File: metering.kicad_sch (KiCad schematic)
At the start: 1 part, among them U1 NodeMCU v2

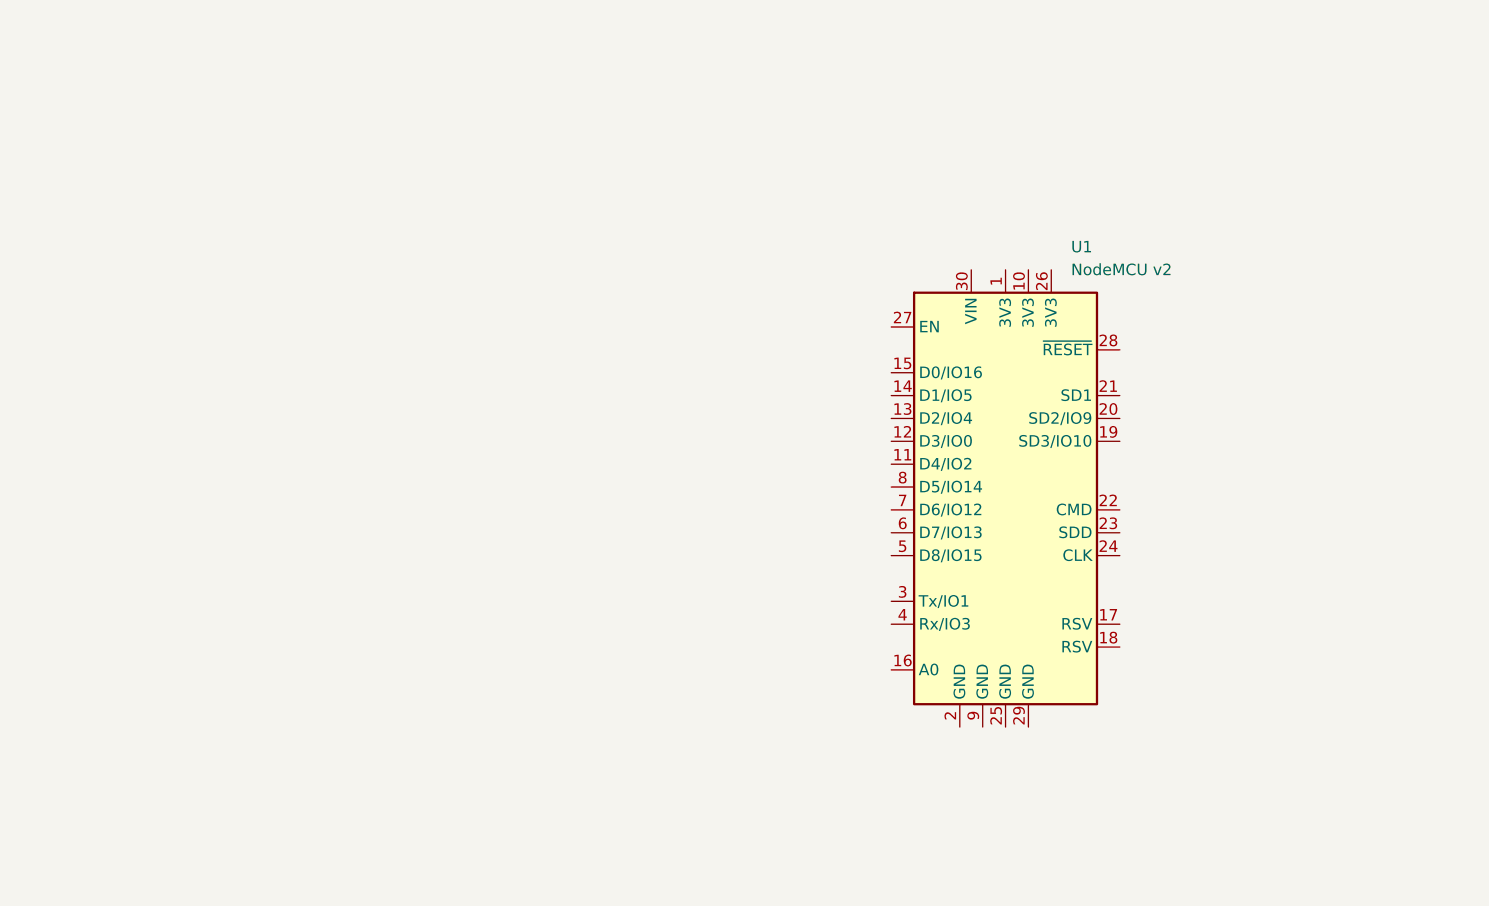
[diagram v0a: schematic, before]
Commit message: Add schematics for electric and gas meter as built in 11/2022
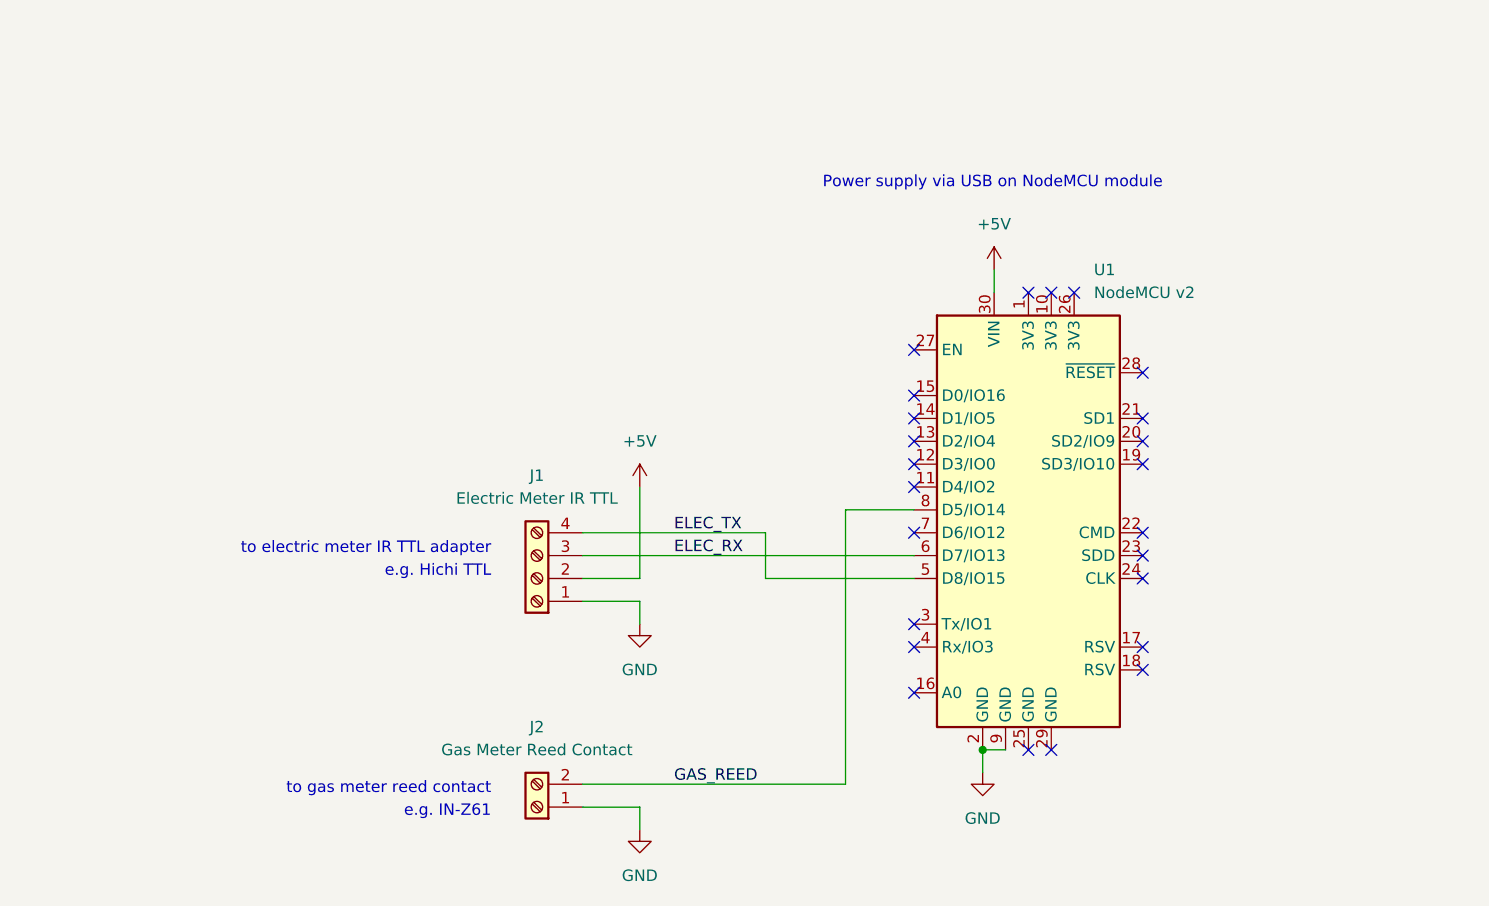
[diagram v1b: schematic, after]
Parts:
- added J1: Electric Meter IR TTL, Connector_PinSocket_2.54mm:PinSocket_1x04_P2.54mm_Vertical, symbol Connector:Screw_Terminal_01x04
- added J2: Gas Meter Reed Contact, Connector_PinSocket_2.54mm:PinSocket_1x02_P2.54mm_Vertical, symbol Connector:Screw_Terminal_01x02
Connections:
- net GND: now reaches U1.2 (GND)
- net GND: now also U1.9 (GND), J1.1 (Pin_1), J2.1 (Pin_1)
- net +5V: now reaches U1.30 (VIN)
- net +5V: now also J1.2 (Pin_2)
- net ELEC_TX: now reaches U1.5 (D8/IO15)
- net ELEC_TX: now also J1.4 (Pin_4)
- net ELEC_RX: now reaches U1.6 (D7/IO13)
- net ELEC_RX: now also J1.3 (Pin_3)
- net GAS_REED: now reaches U1.8 (D5/IO14)
- net GAS_REED: now also J2.2 (Pin_2)
- no-connect marks 0 -> 24
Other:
- note added: "Power supply via USB on NodeMCU module"
- note added: "e.g. Hichi TTL"
- note added: "e.g. IN-Z61"
- note added: "to electric meter IR TTL adapter"
- note added: "to gas meter reed contact"
- title: Smart Home Metering -> Smart Home Energy Metering
- moved on the sheet: U1

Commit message: Add NodeMCU footprint
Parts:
- U1: footprint Module:Arduino_Nano -> NodeMCU_v2:NodeMCU_v2; symbol NodeMCU v2:NodeMCU v2 -> NodeMCU_v2:NodeMCU_v2
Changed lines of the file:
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@@
     )
   )
-  (symbol (lib_id "NodeMCU v2:NodeMCU v2") (at 144.78 82.55 0) (unit 1)
+  (symbol (lib_id "NodeMCU_v2:NodeMCU_v2") (at 144.78 82.55 0) (unit 1)
     (in_bom yes) (on_board yes) (dnp no) (fields_autoplaced)
     (property "Reference" "U1" (at 152.0541 54.61 0)
@@
       (effects (font (size 1.27 1.27)) (justify left))
     )
-    (property "Footprint" "Module:Arduino_Nano" (at 144.78 82.55 0)
+    (property "Footprint" "NodeMCU_v2:NodeMCU_v2" (at 144.78 121.92 0)
       (effects (font (size 1.27 1.27) italic) hide)
     )
-    (property "Datasheet" "https://www.nodemcu.com/index_en.html" (at 144.78 82.55 0)
+    (property "Datasheet" "https://www.nodemcu.com/index_en.html" (at 144.78 119.38 0)
       (effects (font (size 1.27 1.27)) hide)
     )

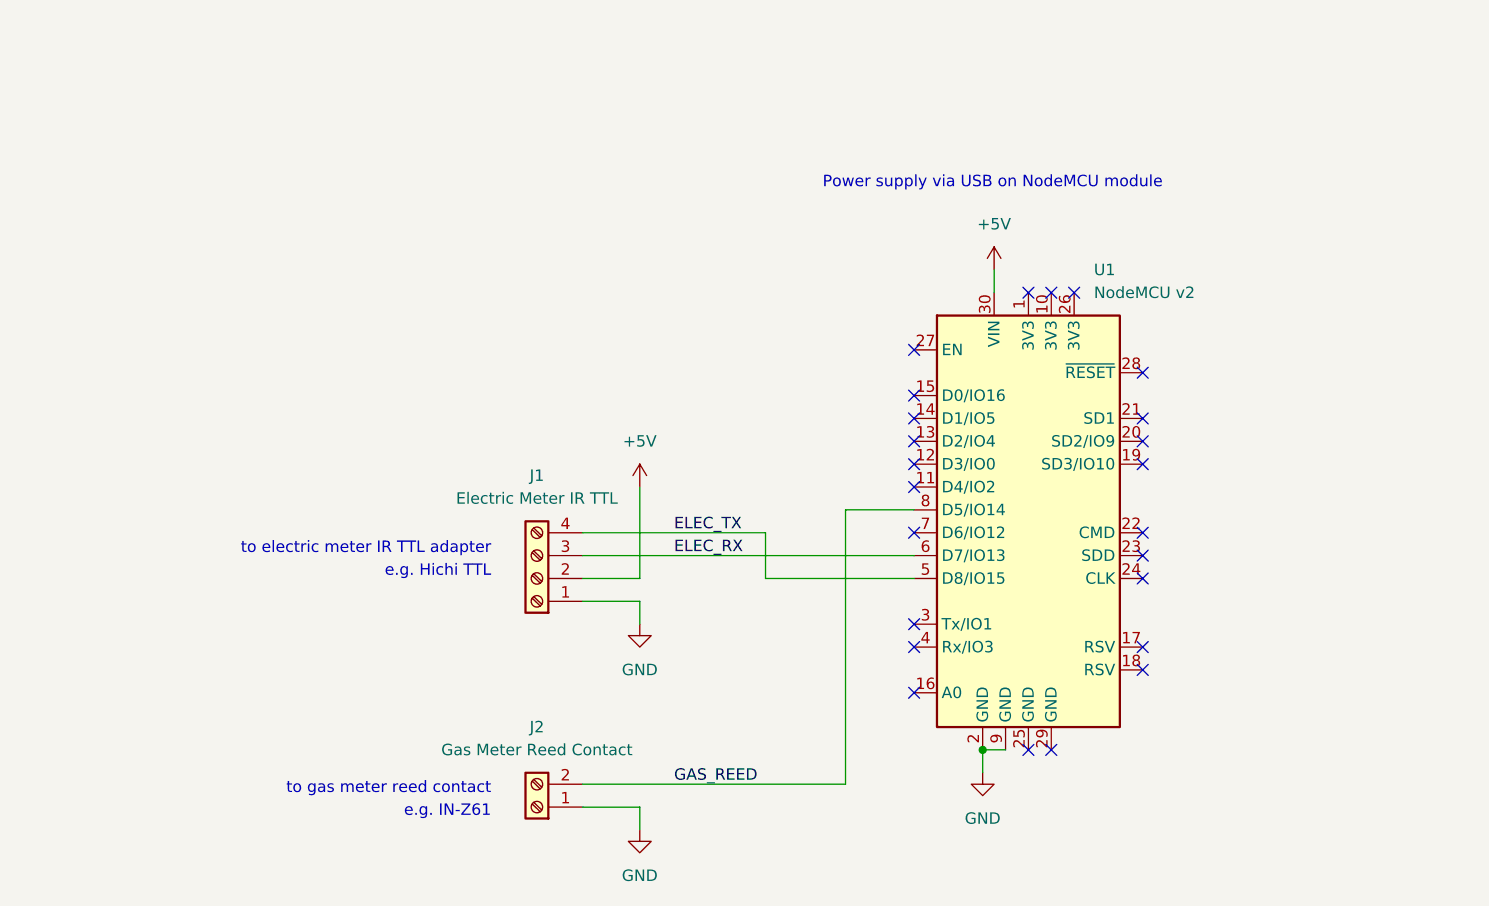
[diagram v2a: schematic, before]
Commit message: Add reed debounce circuit
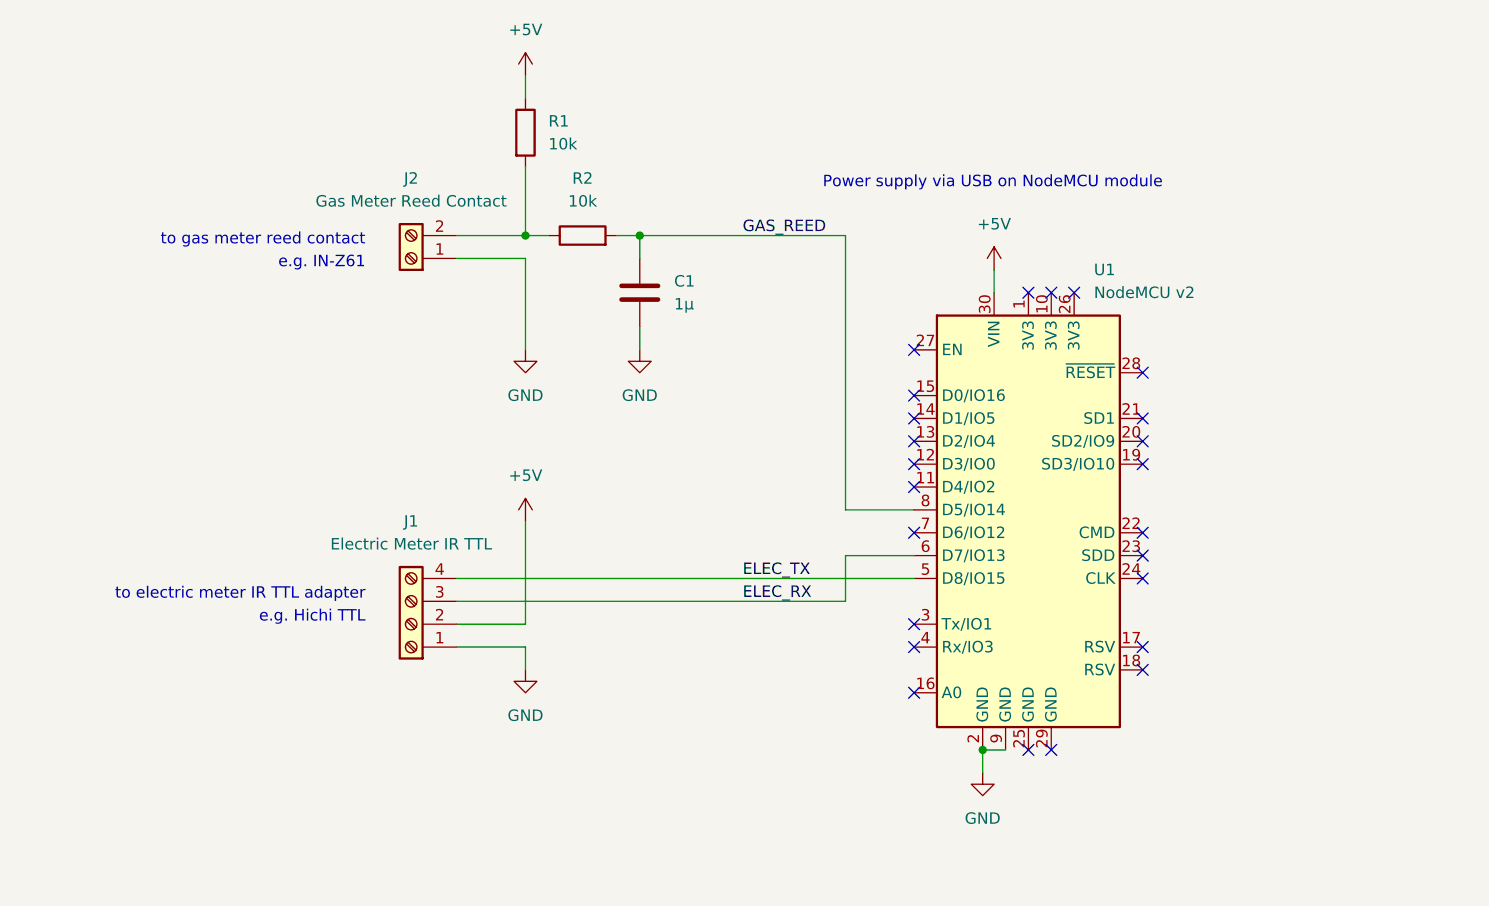
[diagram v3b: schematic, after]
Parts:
- added C1: 1µ, symbol Device:C
- added R1, R2: 10k, symbol Device:R
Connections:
- net +5V: now also R1.1
- net GAS_REED: now also C1.1, R2.2; no longer J2.2 (Pin_2)
- net GND: now also C1.2
- new net: J2.2 (Pin_2), R1.2, R2.1
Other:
- moved on the sheet: J1, J2

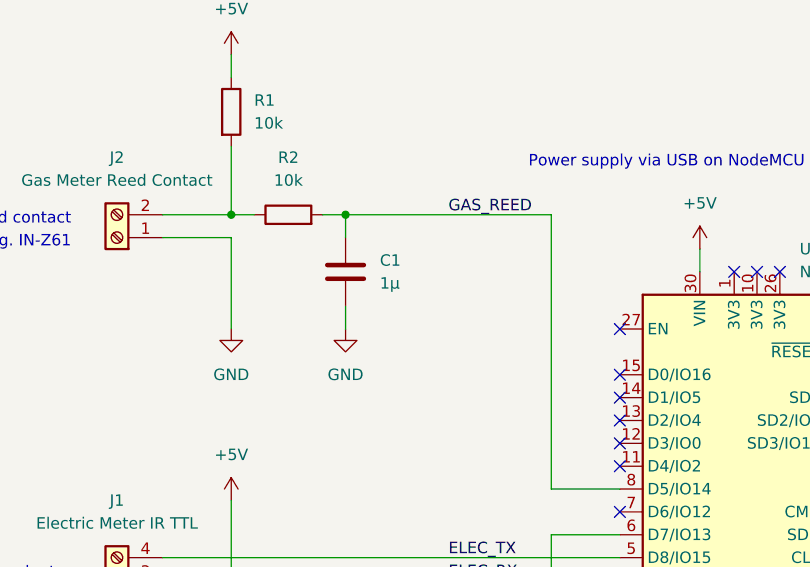
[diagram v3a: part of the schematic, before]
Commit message: Reduce debounce capacitor to 100n
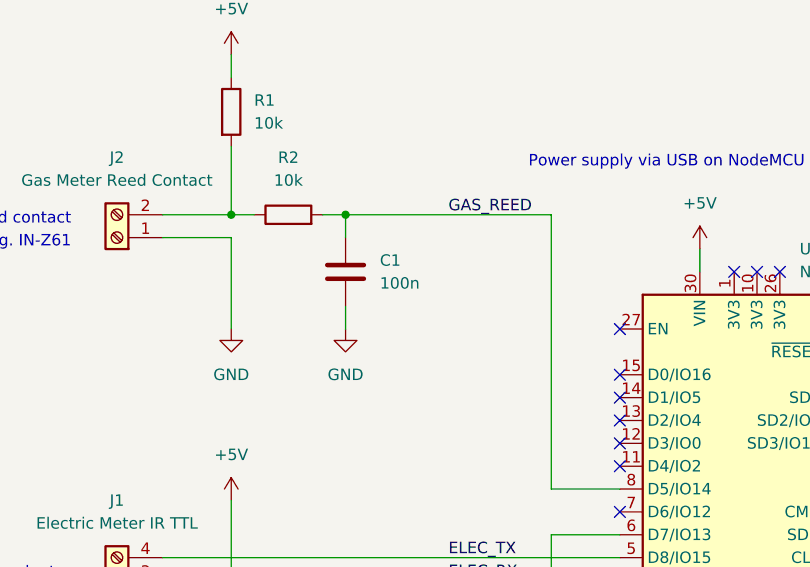
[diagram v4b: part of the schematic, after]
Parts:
- C1: value 1µ -> 100n
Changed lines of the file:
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@@
       (effects (font (size 1.27 1.27)) (justify left))
     )
-    (property "Value" "1µ" (at 105.41 58.42 0)
+    (property "Value" "100n" (at 105.41 58.42 0)
       (effects (font (size 1.27 1.27)) (justify left))
     )

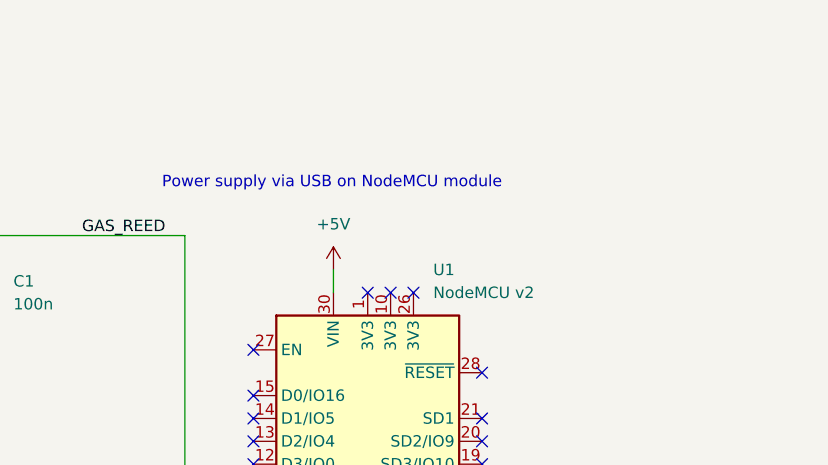
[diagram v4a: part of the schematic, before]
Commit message: Add remark about required diode for external VIN
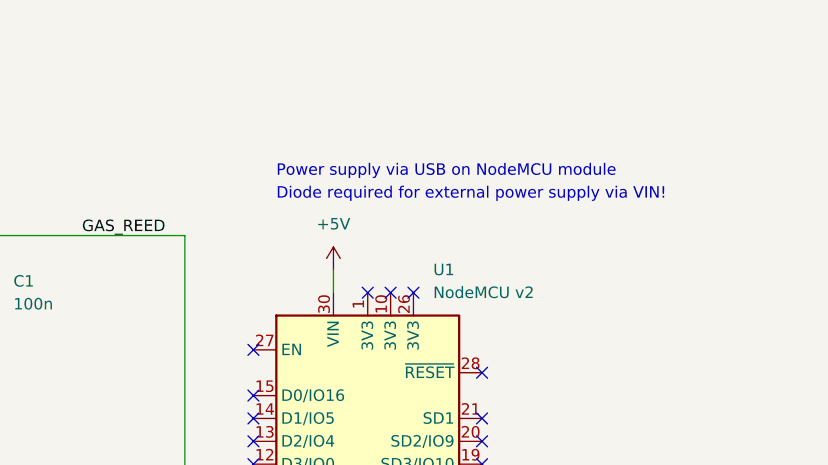
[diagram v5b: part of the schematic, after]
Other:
- note added: "Diode required for external power supply via VIN!"
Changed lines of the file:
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@@
     (stroke (width 0) (type default))
   )
-  (text "Power supply via USB on NodeMCU module" (at 121.92 45.72 0)
+  (text "Power supply via USB on NodeMCU module" (at 134.62 44.45 0)
     (effects (font (size 1.27 1.27)) (justify left bottom))
   )
@@
     (effects (font (size 1.27 1.27)) (justify right bottom))
   )
+  (text "Diode required for external power supply via VIN!" (at 134.62 46.99 0)
+    (effects (font (size 1.27 1.27)) (justify left bottom))
+  )
   (text "e.g. Hichi TTL" (at 71.12 93.98 0)
